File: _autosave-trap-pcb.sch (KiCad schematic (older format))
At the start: 80 parts, among them J1 Conn_01x15, J2 Conn_01x15, M1 Motor_DC, Q1 Q_NMOS_GSD, Q2 Q_NMOS_GSD, Q3 Q_NMOS_GSD, Q4 Q_NMOS_GSD, Q5 Q_NMOS_GSD, Q6 Q_NMOS_GSD, Q7 Q_NMOS_GSD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

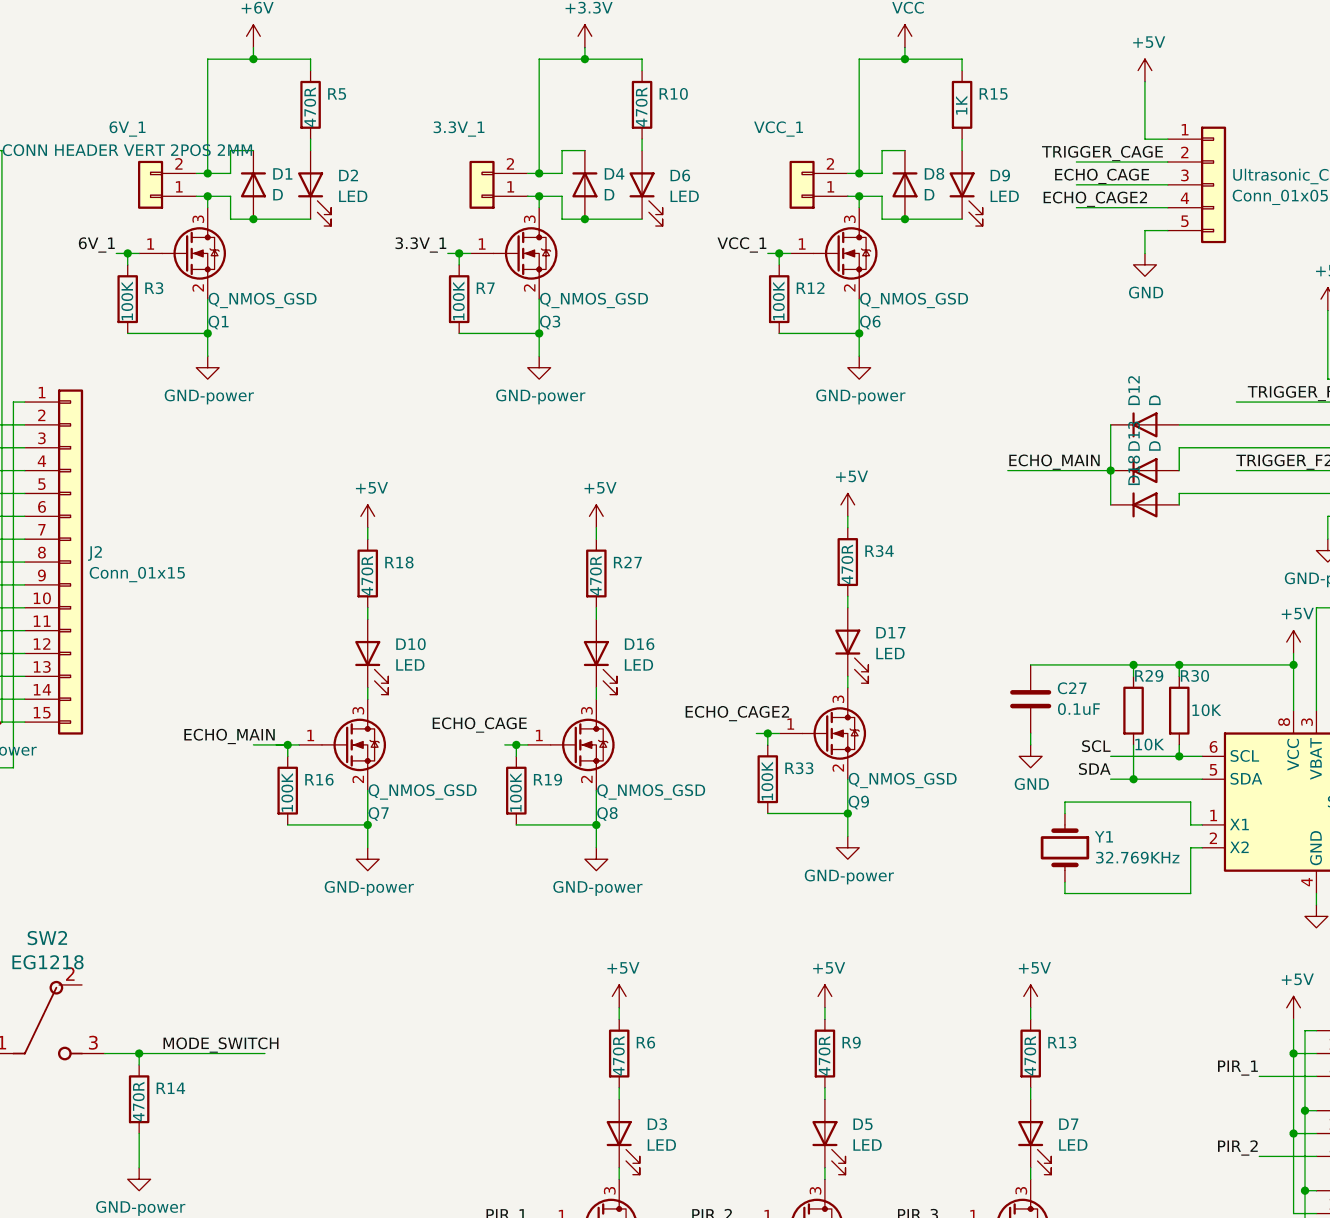
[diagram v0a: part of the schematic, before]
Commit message: DRC Fixes
Fixed DRC errors. Changed connectors to JST.
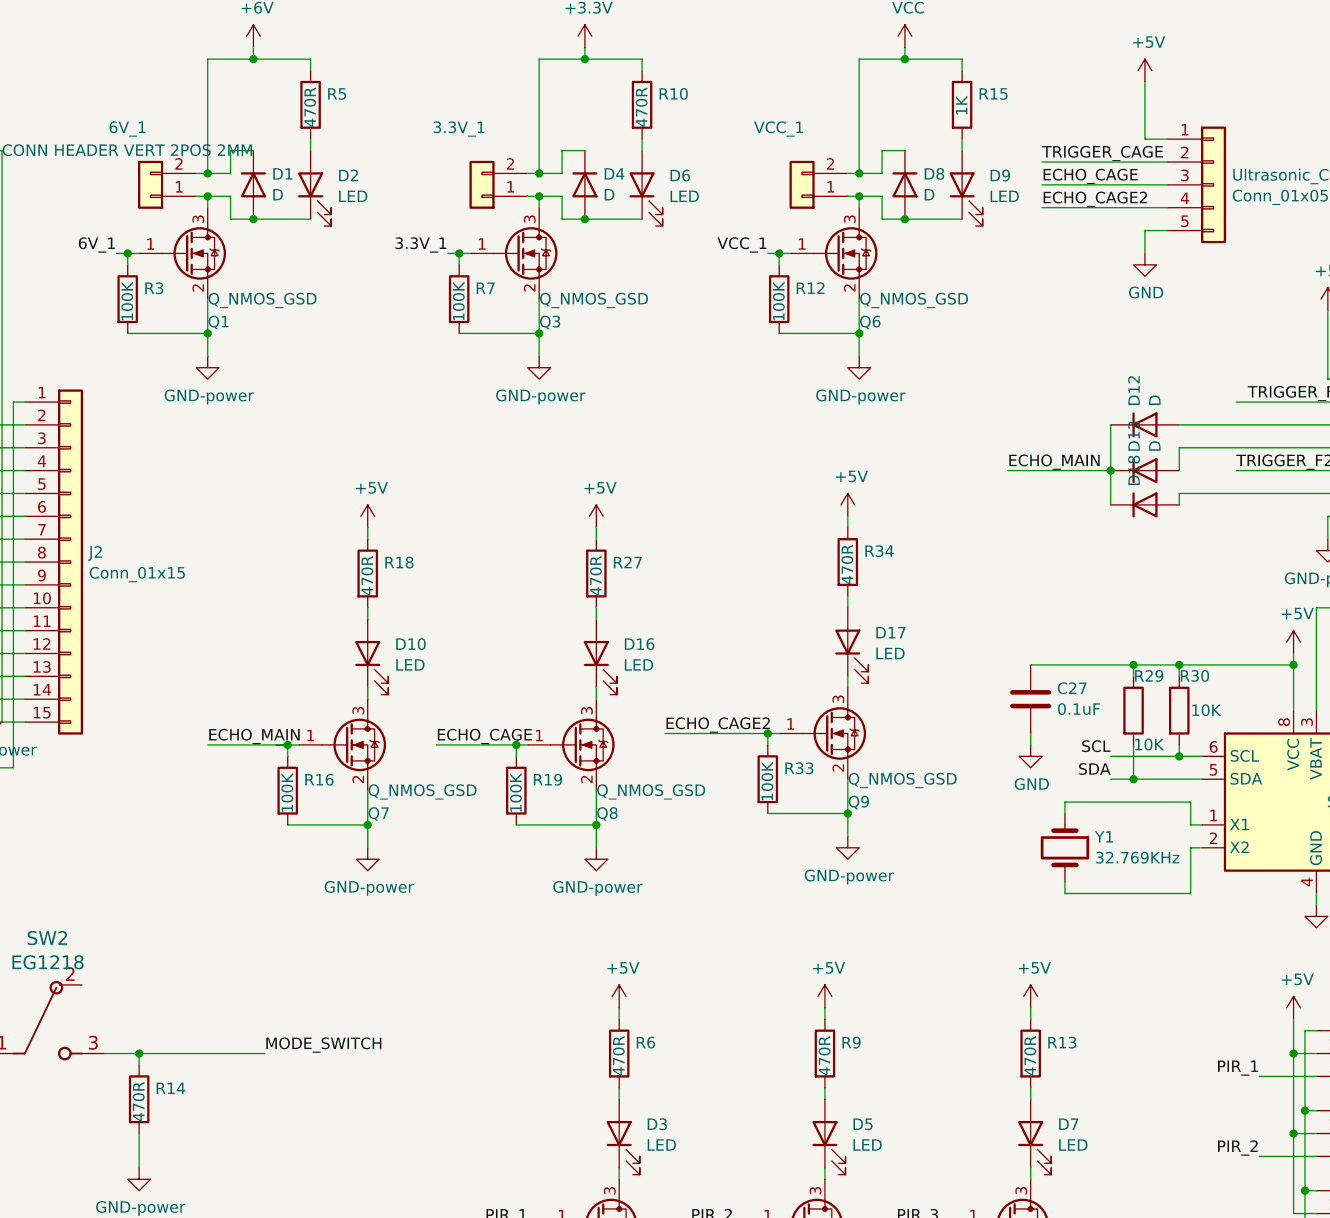
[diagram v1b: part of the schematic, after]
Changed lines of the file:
@@
 Wire Wire Line
 	9400 1550 9500 1550
-Wire Wire Line
-	9500 1250 9100 1250
-Wire Wire Line
-	9500 1350 9100 1350
-Wire Wire Line
-	9500 1450 9100 1450
 $Comp
 L trap-pcb-rescue:GND-power-trap-pcb-rescue #PWR0120
@@
 	1    0    0    -1
 $EndComp
-Text Label 5100 5150 0    50   ~ 0
-MODE_SWITCH
 $Comp
 L trap-pcb-rescue:+5V-power #PWR0121
@@
 Wire Wire Line
 	6000 3200 6000 3250
-Text Label 5600 3800 2    50   ~ 0
-ECHO_MAIN
 Wire Wire Line
 	5650 3850 5650 3800
@@
 Wire Wire Line
 	7000 3200 7000 3250
-Text Label 6700 3750 2    50   ~ 0
-ECHO_CAGE
-Wire Wire Line
-	6600 3800 6650 3800
 Wire Wire Line
 	6650 3850 6650 3800
@@
 Wire Wire Line
 	8100 3150 8100 3200
-Text Label 7850 3700 2    50   ~ 0
-ECHO_CAGE2
-Wire Wire Line
-	7700 3750 7750 3750
 Wire Wire Line
 	7750 3800 7750 3750
@@
 Wire Wire Line
 	1400 3300 2200 3300
-Text Label 8950 1250 0    50   ~ 0
-TRIGGER_CAGE
-Text Label 9000 1350 0    50   ~ 0
-ECHO_CAGE
-Text Label 8950 1450 0    50   ~ 0
-ECHO_CAGE2
-Wire Wire Line
-	5600 3800 5650 3800
-Wire Wire Line
-	5500 3800 5650 3800
 Connection ~ 5300 1300
 Connection ~ 5300 1400
@@
 Text Label 8800 2600 0    50   ~ 0
 ECHO_MAIN
+Wire Wire Line
+	9500 1250 8950 1250
+Wire Wire Line
+	9500 1350 8950 1350
+Wire Wire Line
+	9500 1450 8950 1450
+Text Label 8950 1250 0    50   ~ 0
+TRIGGER_CAGE
+Text Label 8950 1350 0    50   ~ 0
+ECHO_CAGE
+Text Label 8950 1450 0    50   ~ 0
+ECHO_CAGE2
+Text Label 5550 5150 0    50   ~ 0
+MODE_SWITCH
+Wire Wire Line
+	5600 3800 5650 3800
+Wire Wire Line
+	6300 3800 6650 3800
+Wire Wire Line
+	5300 3800 5650 3800
+Text Label 6300 3800 0    50   ~ 0
+ECHO_CAGE
+Text Label 5300 3800 0    50   ~ 0
+ECHO_MAIN
+Wire Wire Line
+	7300 3750 7750 3750
+Text Label 7300 3750 0    50   ~ 0
+ECHO_CAGE2
 $EndSCHEMATC
